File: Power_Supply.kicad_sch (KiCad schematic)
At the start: 80 parts, among them J16 Conn_02x05_Odd_Even, J17 TS NORMAL, J18 EXTERNAL THERMISTOR GND, J22 2S 1.5MHz 2A ICHG, J23 3S 1.5MHz 1A ICHG, J24 4S 1.5MHz 1A ICHG, J25 SYSTEM GND, J26 BATTERY GND, U2 TPS25750DRJKR, U22 TLV75533PDBVR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

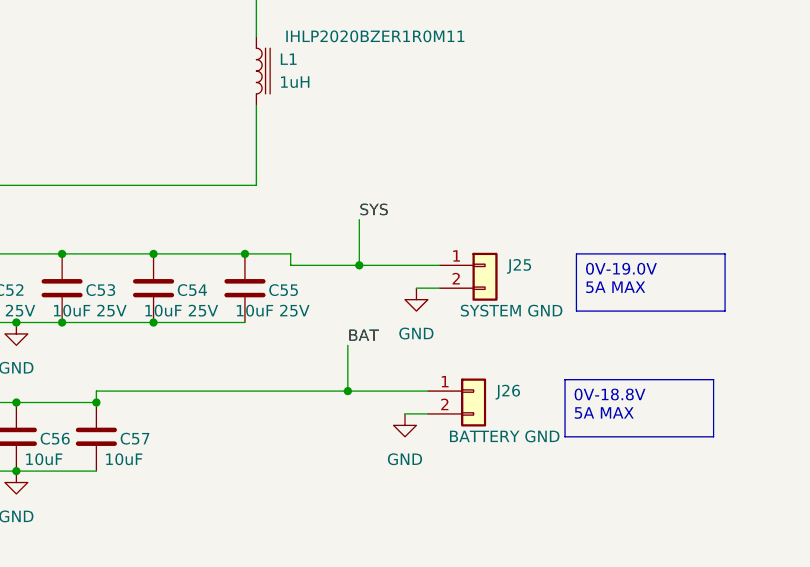
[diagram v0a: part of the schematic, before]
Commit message: more work on custom usb-c power
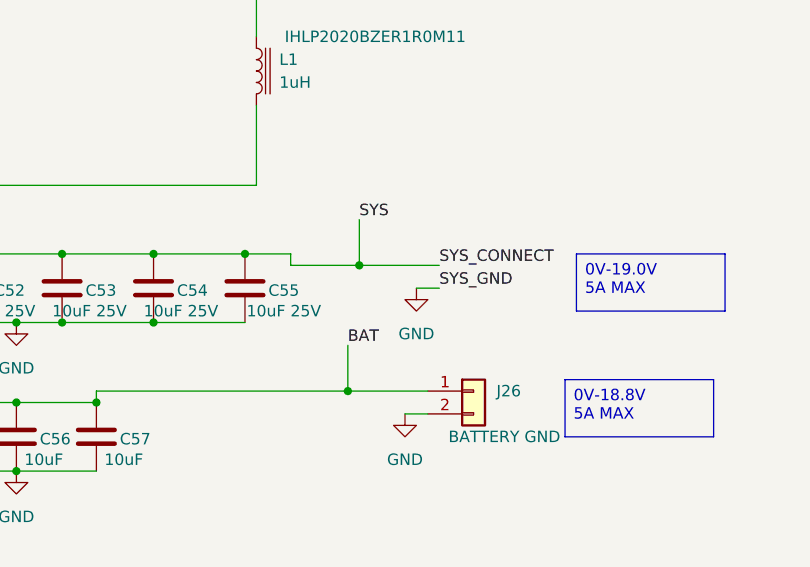
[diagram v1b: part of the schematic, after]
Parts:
- removed J25: SYSTEM GND, symbol Connector_Generic:Conn_01x02
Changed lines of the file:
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@@
 	(generator "eeschema")
 	(generator_version "9.0")
-	(paper "A2")
+	(paper "A1")
 	(text_box "500mA IINDPM"
 		(exclude_from_sim no)
@@
 		)
 	)
+	(label "SYS_GND"
+		(at 212.09 232.41 0)
+		(effects
+			(font
+				(size 1.27 1.27)
+			)
+			(justify left bottom)
+		)
+	)
 	(label "LDO_3V3"
 		(at 138.43 283.21 180)
@@
 		)
 	)
+	(label "SYS_CONNECT"
+		(at 212.09 229.87 0)
+		(effects
+			(font
+				(size 1.27 1.27)
+			)
+			(justify left bottom)
+		)
+	)
 	(label "STAT"
 		(at 128.27 261.62 0)
@@
 	)
 	(symbol
-		(lib_id "Connector_Generic:Conn_01x02")
-		(at 217.17 229.87 0)
-		(unit 1)
-		(exclude_from_sim no)
-		(in_bom yes)
-		(on_board yes)
-		(dnp no)
-		(property "Reference" "J25"
-			(at 219.71 229.8699 0)
-			(effects
-				(font
-					(size 1.27 1.27)
-				)
-				(justify left)
-			)
-		)
-		(property "Value" "SYSTEM GND"
-			(at 214.376 234.95 0)
-			(effects
-				(font
-					(size 1.27 1.27)
-				)
-				(justify left)
-			)
-		)
-		(property "Footprint" ""
-			(at 217.17 229.87 0)
-			(effects
-				(font
-					(size 1.27 1.27)
-				)
-				(hide yes)
-			)
-		)
-		(property "Datasheet" "~"
-			(at 217.17 229.87 0)
-			(effects
-				(font
-					(size 1.27 1.27)
-				)
-				(hide yes)
-			)
-		)
-		(property "Description" "Generic connector, single row, 01x02, script generated (kicad-library-utils/schlib/autogen/connector/)"
-			(at 217.17 229.87 0)
-			(effects
-				(font
-					(size 1.27 1.27)
-				)
-				(hide yes)
-			)
-		)
-		(pin "2"
-		)
-		(pin "1"
-		)
-		(instances
-			(project "microcyber"
-				(path "/7ac319af-771c-4997-a005-b73a4a9b44ab/6ab392bb-0c5a-4b0d-a4a4-2c62db1aa129"
-					(reference "J25")
-					(unit 1)
-				)
-			)
-		)
-	)
-	(symbol
 		(lib_id "Library:GND")
 		(at 209.55 232.41 0)
@@
 		)
 		(property "Value" "10uF 25V"
-			(at 193.548 234.95 0)
+			(at 194.818 234.95 0)
 			(effects
 				(font
